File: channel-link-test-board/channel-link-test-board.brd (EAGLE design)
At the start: 124 x 95 mm, 60 parts, among them U1 DS90CR217MTD/NOPBMTD48_TEX-L, U2 DS90CR218AMTD/NOPBMTD48_TEX-L

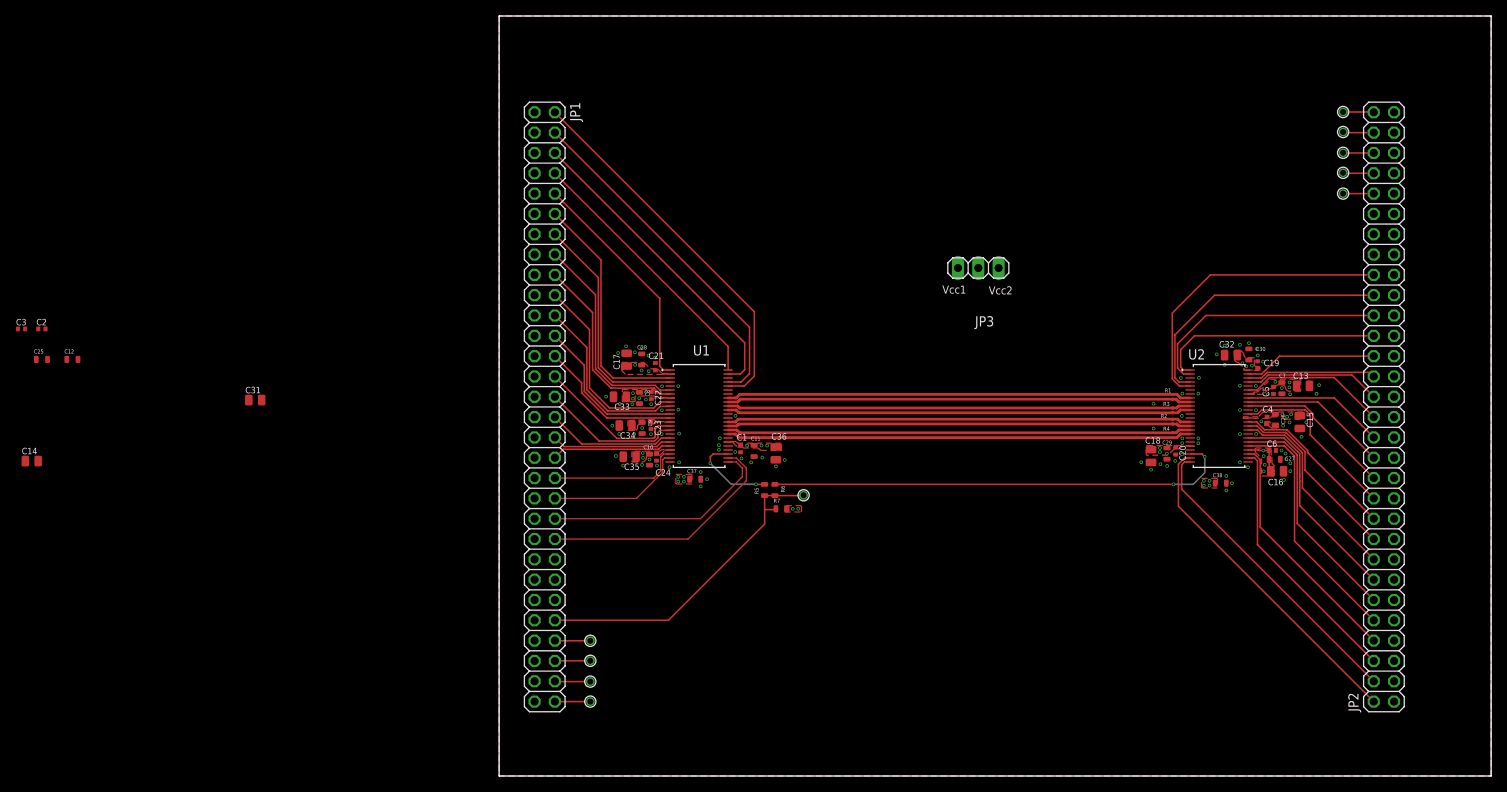
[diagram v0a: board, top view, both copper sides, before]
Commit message: minor cleanup, ground stitching, attributes
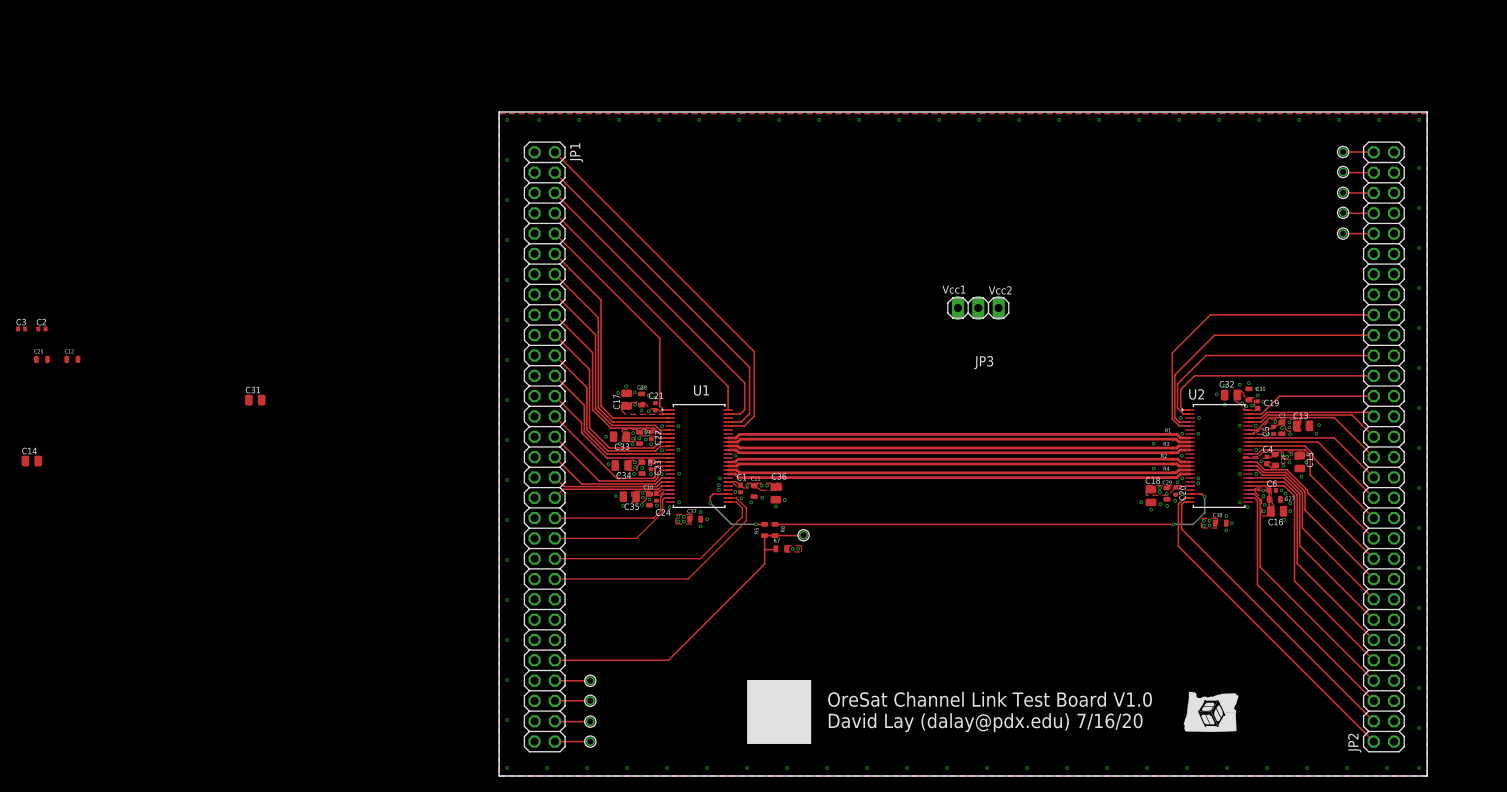
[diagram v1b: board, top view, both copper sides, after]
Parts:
- R7: value 100 -> 10k
- moved C34 5.02 mm to (15.3, 38.8)
- moved TP1 5.00 mm to (38.1, 30.1)
- moved TP5 5.00 mm to (11.4, 6.80)
- moved TP6 5.00 mm to (11.4, 4.30)
- moved C1 5.00 mm to (30.2, 35.9)
- moved C10 5.00 mm to (18.8, 34.6)
- moved C11 5.00 mm to (31.9, 35.6)
- moved C13 5.00 mm to (100.5, 43.8)
- moved C15 5.00 mm to (100.1, 39.2)
- moved C16 5.00 mm to (97.2, 33.1)
- moved C17 5.00 mm to (15.9, 47.0)
- moved C18 5.00 mm to (81.5, 35.0)
- moved C19 5.00 mm to (94.8, 46.4)
- moved C20 5.00 mm to (84.6, 35.6)
- moved C21 5.00 mm to (19.5, 46.2)
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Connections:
- removed net N$46: JP2.1, JP2.11, JP2.13, JP2.15, JP2.17, JP2.19, JP2.21, JP2.23, JP2.25, JP2.27, JP2.29, JP2.3, JP2.31, JP2.33, JP2.35, JP2.37, JP2.39, JP2.41, JP2.43, JP2.45, JP2.46, JP2.5, JP2.7, JP2.9
- net GND: now also JP2.1, JP2.11, JP2.13, JP2.15, JP2.17, JP2.19, JP2.21, JP2.23, JP2.25, JP2.27, JP2.29, JP2.3, JP2.31, JP2.33, JP2.35, JP2.37, JP2.39, JP2.41, JP2.43, JP2.45, JP2.46, JP2.5, JP2.7, JP2.9
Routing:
- net NUCLEOSUPPLY: track 79.6 -> 76.6 mm
- net 3.3V: vias 37 -> 39
- added copper zone on layer 15, net A8SUPPLY
- added copper zone on layer 15, net GND
- added copper zone on layer 15, net NUCLEOSUPPLY
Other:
- board size 124 x 95 mm -> 116 x 83 mm
- board text added: "OreSat Channel Link Test Board V1.0 David Lay (dalay@pdx.edu) 7/16/20"

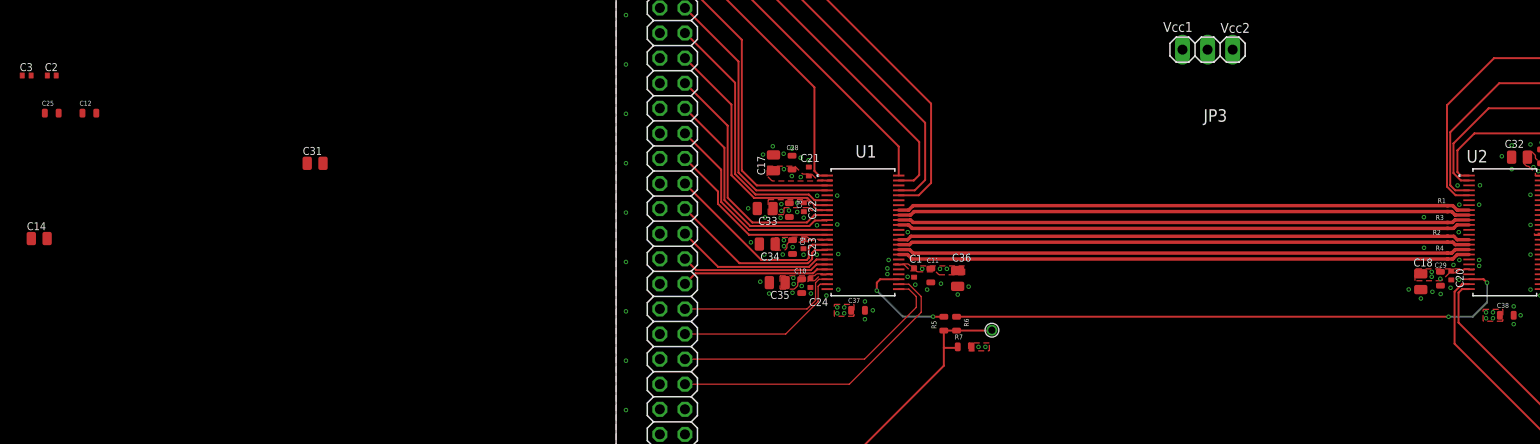
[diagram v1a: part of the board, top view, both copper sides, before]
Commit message: moved LVDS lines so I could bypass the LVDS VCC
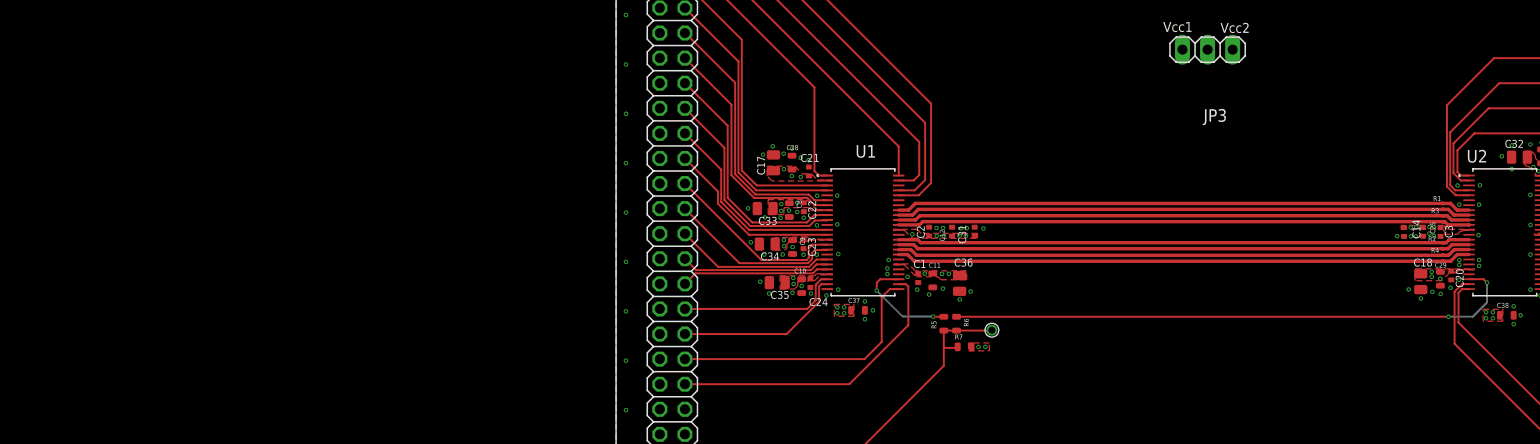
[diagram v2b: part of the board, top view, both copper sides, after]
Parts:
- C12, C25: device oresat-rcl:.0603-C-NOSILK -> oresat-rcl:.0402-C-NOSILK
- C14, C31: device oresat-rcl:.0805-C-NOSILK -> oresat-rcl:.0402-C-NOSILK
- moved C3 144.1 mm to (83.5, 40.0), turned to 270 degrees
- moved C25 139.4 mm to (81.7, 40.1), turned to 270 degrees
- moved C14 138.2 mm to (79.8, 40.0), turned to 270 degrees
- moved C2 90.3 mm to (31.7, 40.1), turned to 90 degrees
- moved C12 88.2 mm to (34.0, 40.1), turned to 90 degrees
- moved C31 67.1 mm to (36.3, 40.1), turned to 90 degrees
- moved R3 0.83 mm to (83.7, 41.4)
- moved R2 0.79 mm to (83.7, 38.7)
- moved C1 0.69 mm to (30.6, 35.4)
- moved C11 0.54 mm to (32.1, 35.1)
- moved C36 0.54 mm to (34.8, 34.8)
- moved R4 0.52 mm to (83.7, 37.4)
- moved R1 0.52 mm to (83.7, 42.6)
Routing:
- net NUCLEOSUPPLY: track 76.6 -> 89.7 mm
- net N$29: track 28.8 -> 27.2 mm
- net N$30: track 31.3 -> 30.1 mm
- net 3.3V: vias 39 -> 48

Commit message: ocd fixes
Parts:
- added TP2, TP7: PTR1B2,54, testpad:B2,54
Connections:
- net N$1 renamed LVDS0-
- net N$2 renamed LVDS0+
- net N$3 renamed LVDS1-
- net N$4 renamed LVDS1+
- net N$5 renamed LVDS2-
- net N$6 renamed LVDS2+
- net N$7 renamed LVDSCLK-
- net N$8 renamed LVDSCLK+
- net N$30: now also TP2.TP
- net N$66: now also TP7.TP
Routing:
- net GND: track 0.00 -> 2.96 mm
- net N$30: track 30.1 -> 31.6 mm
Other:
- board text added: "LVDS Rx"
- board text added: "LVDS Tx"
- board text added: "Rx0"
- board text added: "Rx20"
- board text added: "RxCLKOut"
- board text added: "Tx0"
- board text added: "Tx20"
- board text added: "TxCLKIn"
- board text added: "VccRx"
- board text added: "VccTX"
- board text removed: "Vcc1"
- board text removed: "Vcc2"
